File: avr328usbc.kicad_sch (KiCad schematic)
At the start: 10 parts, among them J1 USB_C_Receptacle, J2 USB_C_Receptacle_PowerOnly_6P, U1 ATmega328P-P, U2 MCP2221AxP, U3 ACPL-772L-000E, U4 ACPL-772L-000E

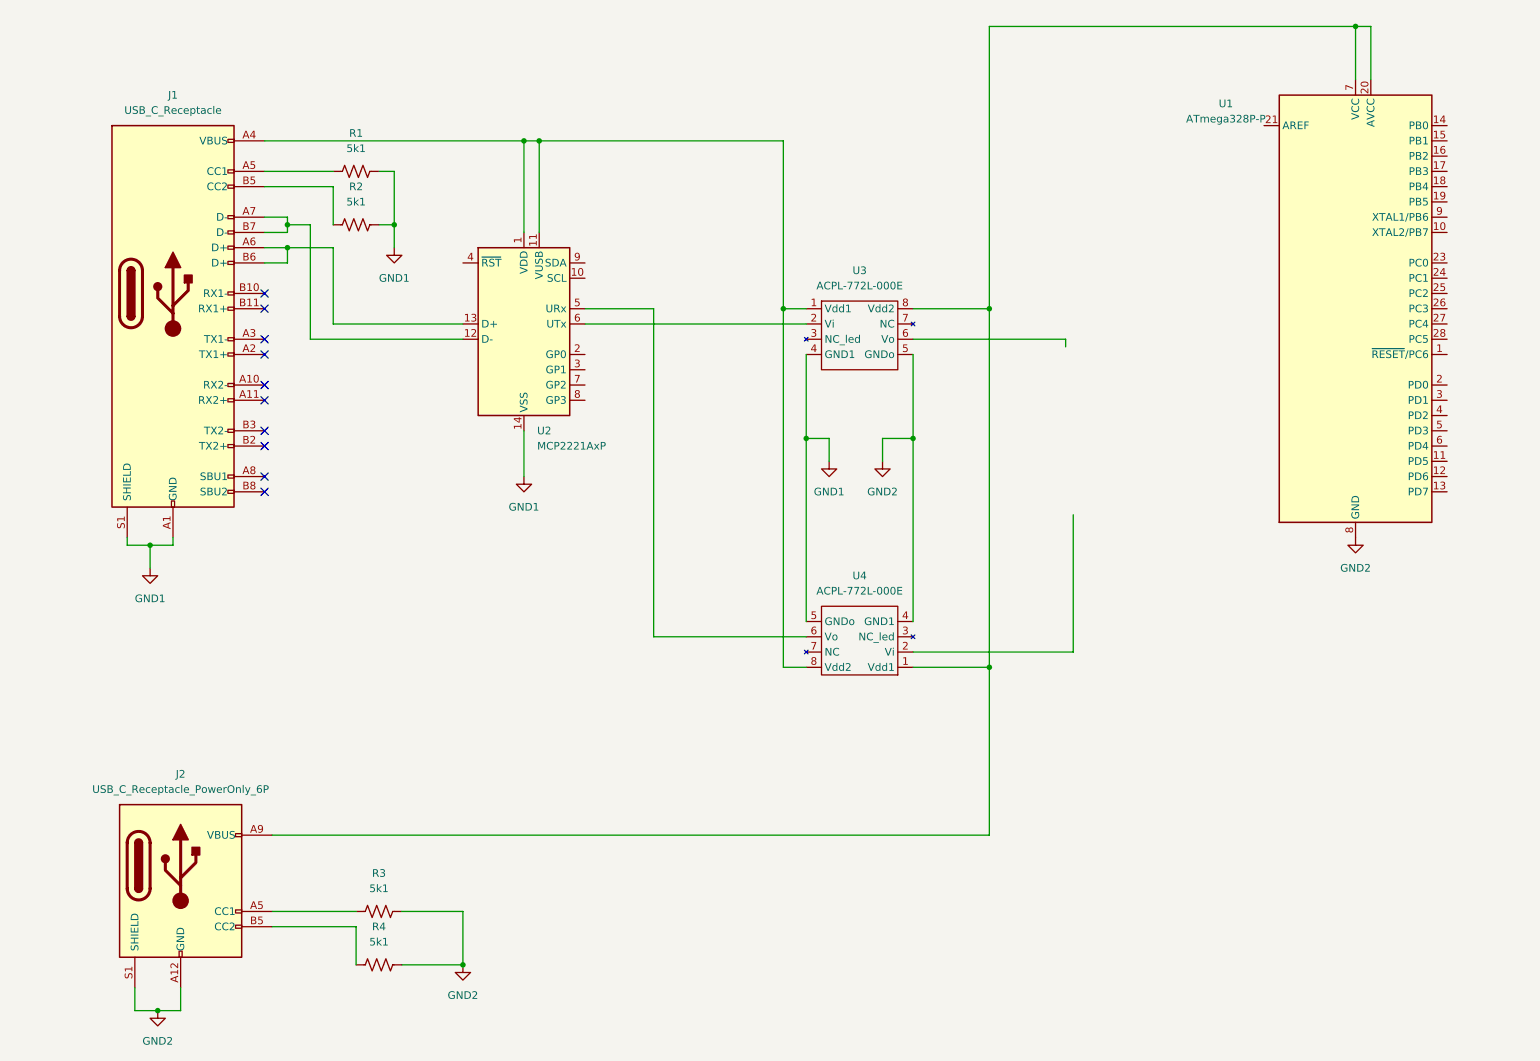
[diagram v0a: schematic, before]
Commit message: schematic: added a bunch of labels & changed pwer to labels
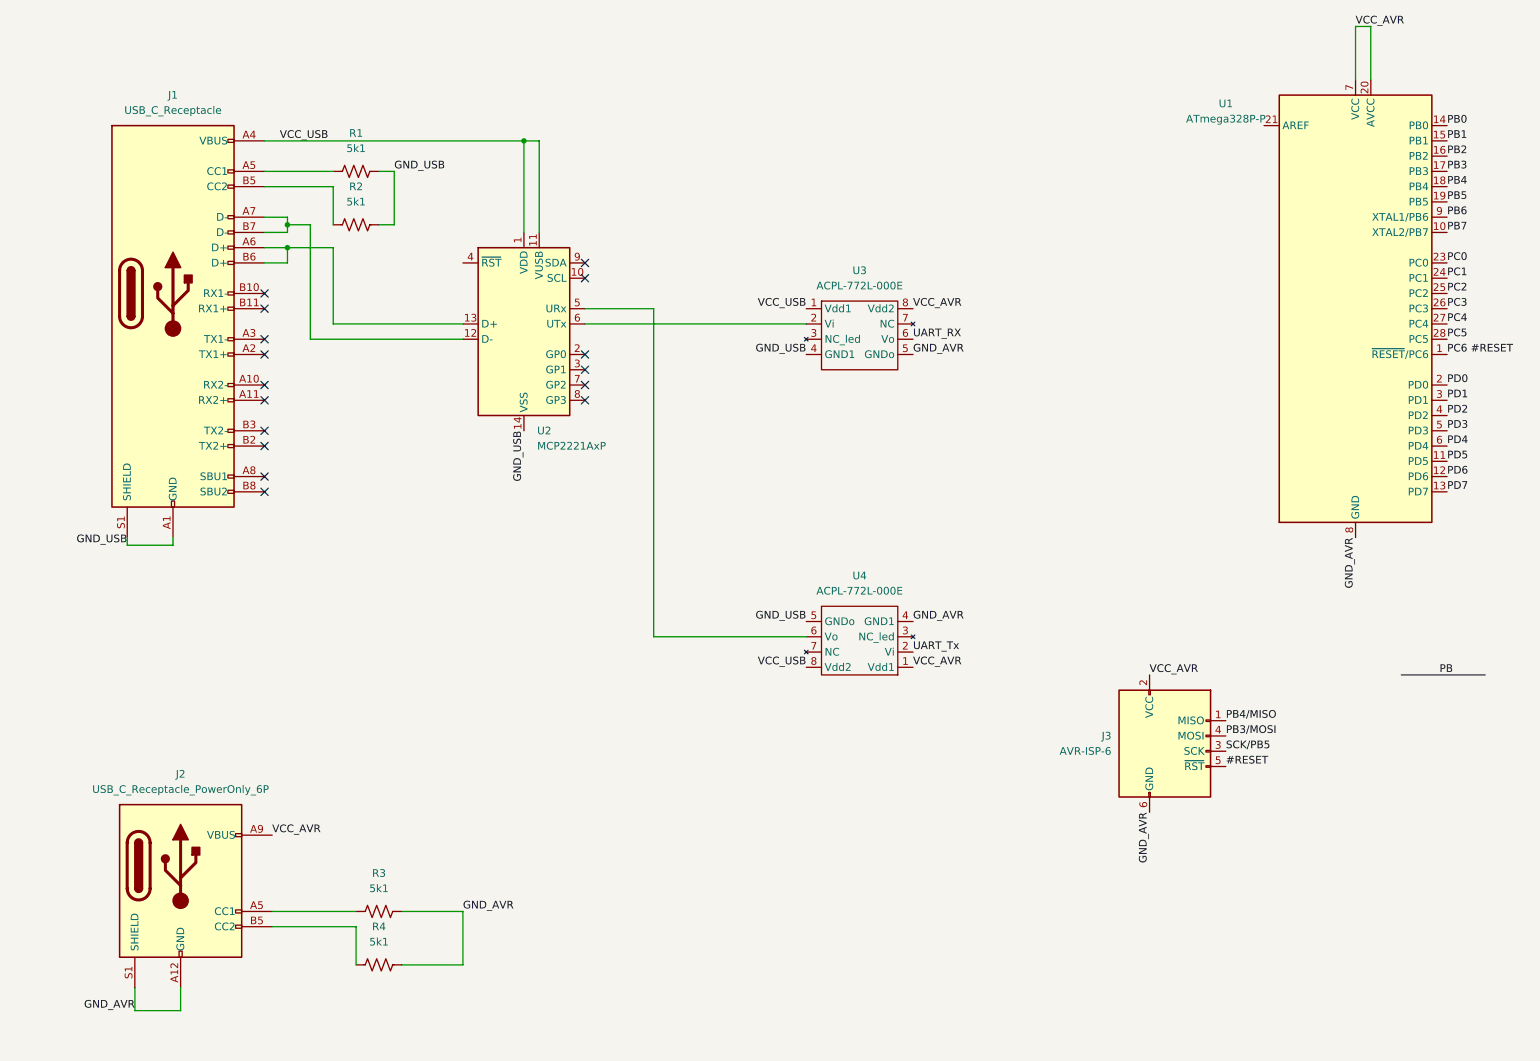
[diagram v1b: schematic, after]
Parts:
- added J3: AVR-ISP-6, symbol Connector:AVR-ISP-6
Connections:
- net VCC_AVR: now reaches J2.A9 (VBUS), J2.B9 (VBUS), U1.20 (AVCC), U1.7 (VCC), U3.8 (Vdd2), U4.1 (Vdd1)
- net VCC_AVR: now also J3.2 (VCC)
- net UART_Tx: now reaches U4.2 (Vi)
- net VCC_USB: now reaches J1.A4 (VBUS), J1.A9 (VBUS), J1.B4 (VBUS), J1.B9 (VBUS), U2.1 (VDD), U2.11 (VUSB), U3.1 (Vdd1), U4.8 (Vdd2)
- net PC6 #RESET: now reaches U1.1 (~{RESET}/PC6)
- net PB7: now reaches U1.10 (XTAL2/PB7)
- net PD5: now reaches U1.11 (PD5)
- net PD6: now reaches U1.12 (PD6)
- net PD7: now reaches U1.13 (PD7)
- net PB0: now reaches U1.14 (PB0)
- net PB1: now reaches U1.15 (PB1)
- net PB2: now reaches U1.16 (PB2)
- net PB3: now reaches U1.17 (PB3)
- net PB4: now reaches U1.18 (PB4)
- net PB5: now reaches U1.19 (PB5)
- net PD0: now reaches U1.2 (PD0)
- net PC0: now reaches U1.23 (PC0)
- net PC1: now reaches U1.24 (PC1)
- net PC2: now reaches U1.25 (PC2)
- net PC3: now reaches U1.26 (PC3)
- net PC4: now reaches U1.27 (PC4)
- net PC5: now reaches U1.28 (PC5)
- net PD1: now reaches U1.3 (PD1)
- net PD2: now reaches U1.4 (PD2)
- net PD3: now reaches U1.5 (PD3)
- net PD4: now reaches U1.6 (PD4)
- net PB6: now reaches U1.9 (XTAL1/PB6)
- net UART_RX: now reaches U3.6 (Vo)
- net GND1 renamed GND_USB
- net GND2 renamed GND_AVR
- net GND_AVR: now also J3.6 (GND)
- new net #RESET: J3.5 (~{RST})
- new net PB3/MOSI: J3.4 (MOSI)
- new net PB4/MISO: J3.1 (MISO)
- new net SCK/PB5: J3.3 (SCK)
- no-connect marks 10 -> 16

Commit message: added mcu sheet and global labels for power
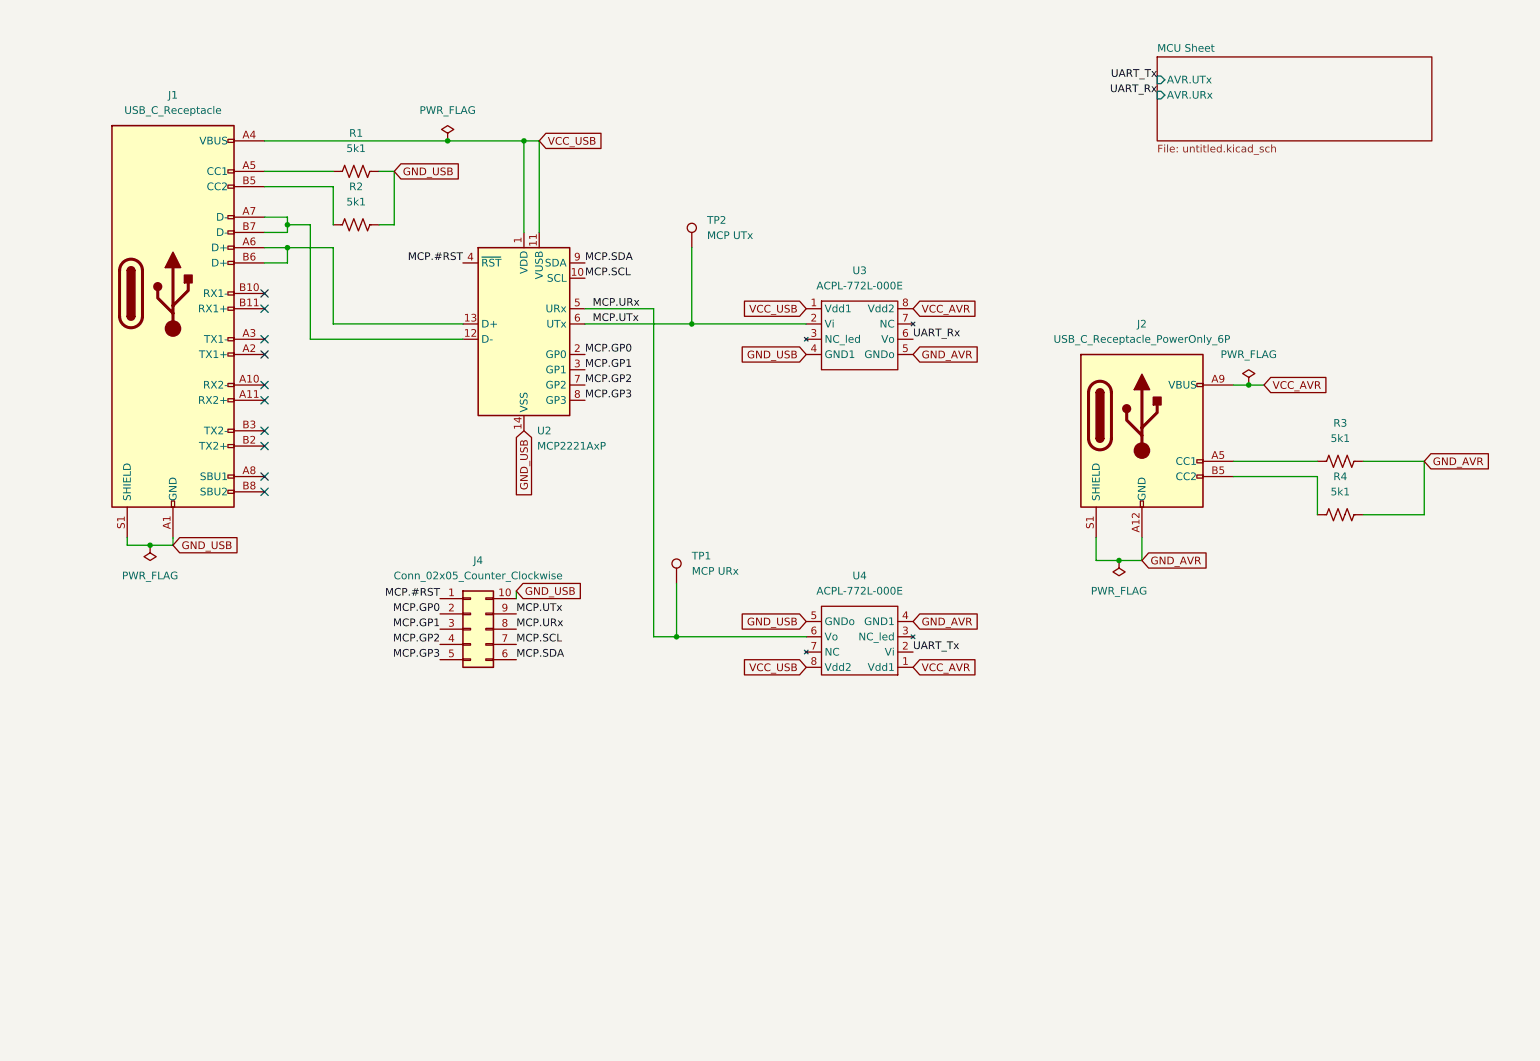
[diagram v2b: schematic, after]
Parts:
- removed J3: AVR-ISP-6, symbol Connector:AVR-ISP-6
- removed U1: ATmega328P-P, Package_DIP:DIP-28_W7.62mm, symbol MCU_Microchip_ATmega:ATmega328P-P
- added J4: Conn_02x05_Counter_Clockwise, symbol Connector_Generic:Conn_02x05_Counter_Clockwise
- added TP1: MCP URx, symbol Connector:TestPoint
- added TP2: MCP UTx, symbol Connector:TestPoint
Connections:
- net GND_USB: now also J4.10 (Pin_10)
- net MCP.URx: now reaches U2.5 (URx), U4.6 (Vo)
- net MCP.URx: now also J4.8 (Pin_8), TP1.1
- net MCP.SCL: now reaches U2.10 (SCL)
- net MCP.SCL: now also J4.7 (Pin_7)
- net MCP.GP0: now reaches U2.2 (GP0)
- net MCP.GP0: now also J4.2 (Pin_2)
- net MCP.GP1: now reaches U2.3 (GP1)
- net MCP.GP1: now also J4.3 (Pin_3)
- net MCP.#RST: now reaches U2.4 (~{RST})
- net MCP.#RST: now also J4.1 (Pin_1)
- net MCP.UTx: now reaches U2.6 (UTx), U3.2 (Vi)
- net MCP.UTx: now also J4.9 (Pin_9), TP2.1
- net MCP.GP2: now reaches U2.7 (GP2)
- net MCP.GP2: now also J4.4 (Pin_4)
- net MCP.GP3: now reaches U2.8 (GP3)
- net MCP.GP3: now also J4.5 (Pin_5)
- net MCP.SDA: now reaches U2.9 (SDA)
- net MCP.SDA: now also J4.6 (Pin_6)
- net UART_RX renamed UART_Rx
- no-connect marks 16 -> 10
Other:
- added sheet MCU Sheet (untitled.kicad_sch)
- company: (none) -> HugonLabs
- title: (none) -> AVR328-USB
- moved on the sheet: J2, R3, R4

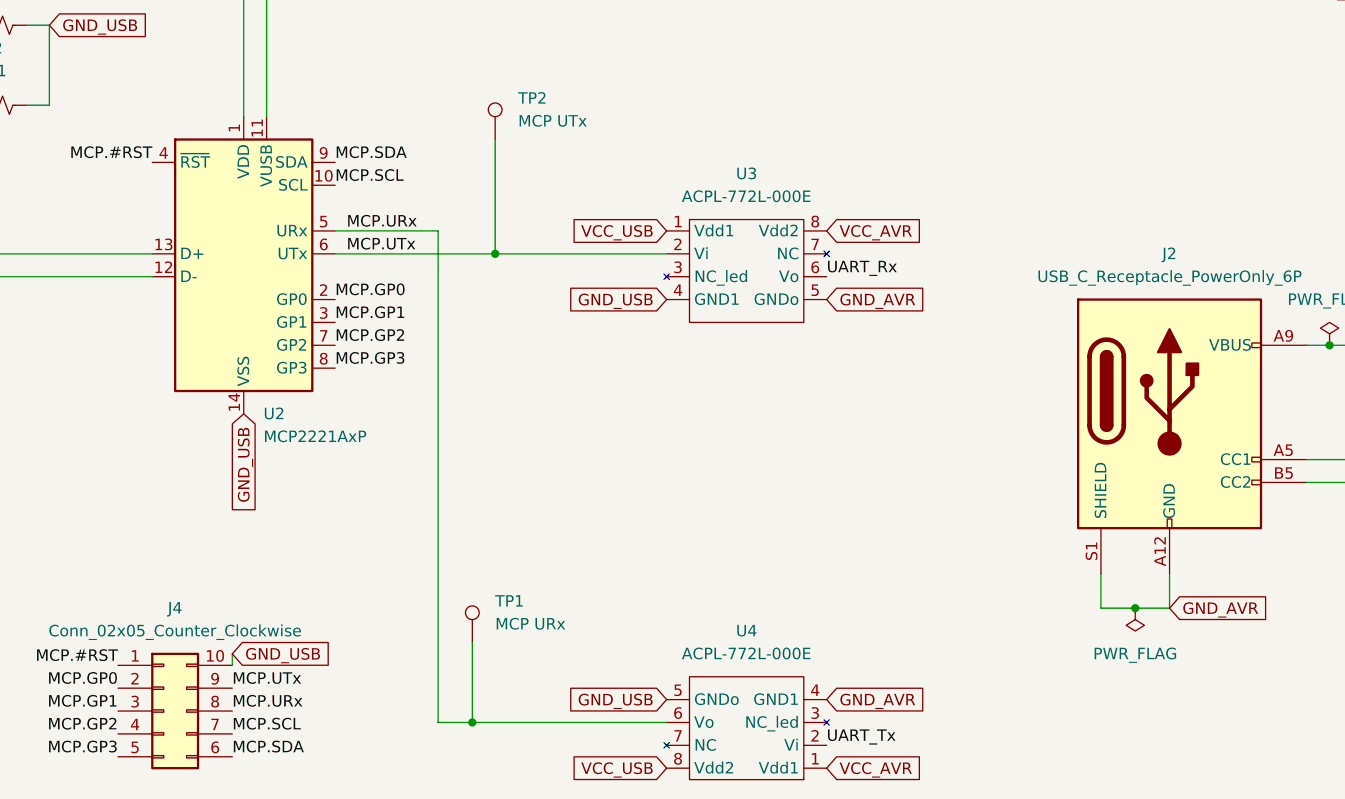
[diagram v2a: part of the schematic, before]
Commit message: sch: finished with main components
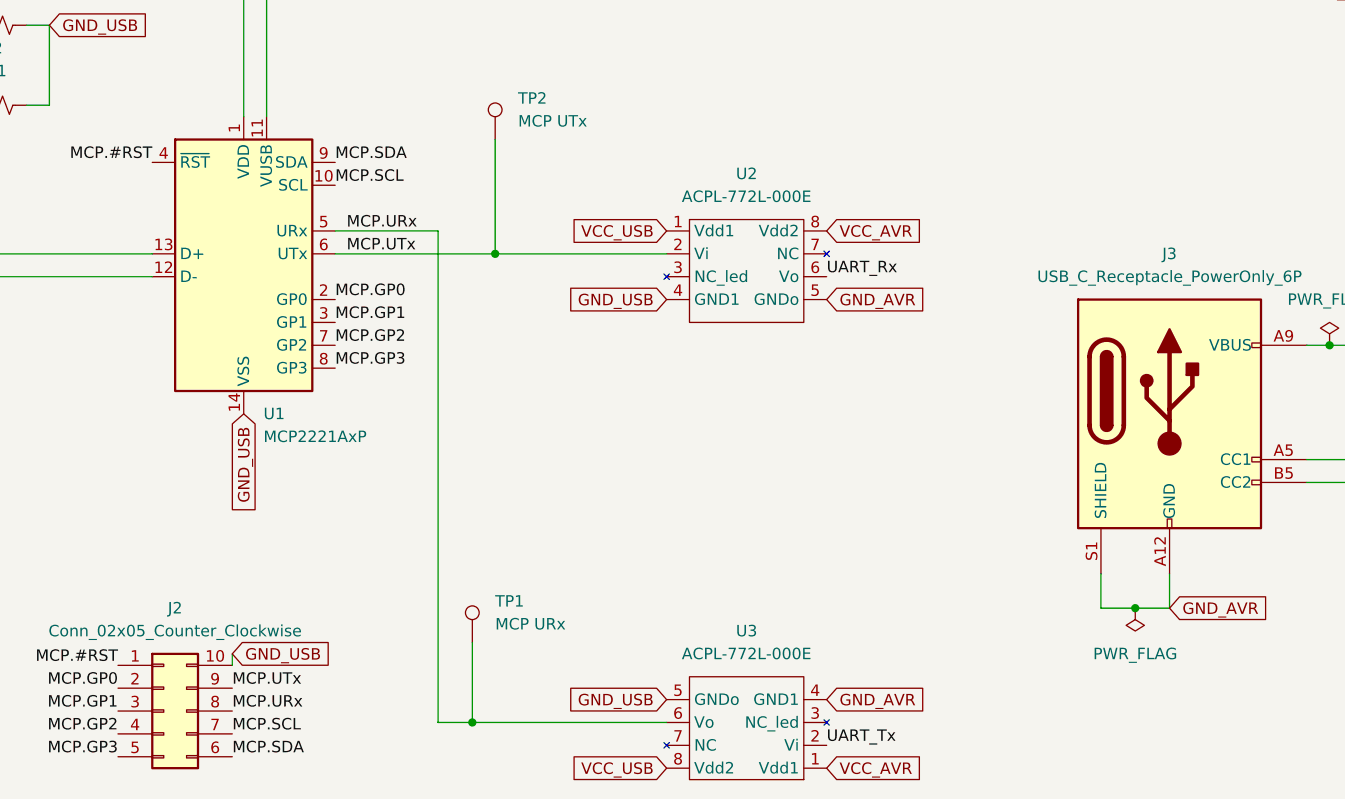
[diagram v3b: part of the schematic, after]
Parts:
- renumbered J4 to J2, J2 to J3, U2 to U1, U3 to U2, U4 to U3
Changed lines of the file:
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@@
 		(dnp no)
 		(fields_autoplaced yes)
-		(property "Reference" "#FLG04"
+		(property "Reference" "#FLG03"
 			(at 204.47 113.665 0)
 			(effects
@@
 			(project "avr328usbc"
 				(path "/e7a067a8-1d75-4b62-a93c-d6508c6150f1"
-					(reference "#FLG04")
+					(reference "#FLG03")
 					(unit 1)
 				)
@@
 		(dnp no)
 		(fields_autoplaced yes)
-		(property "Reference" "J2"
+		(property "Reference" "J3"
 			(at 208.28 72.39 0)
 			(effects
@@
 			(project "avr328usbc"
 				(path "/e7a067a8-1d75-4b62-a93c-d6508c6150f1"
-					(reference "J2")
+					(reference "J3")
 					(unit 1)
 				)
@@
 		(dnp no)
 		(fields_autoplaced yes)
-		(property "Reference" "U4"
+		(property "Reference" "U3"
 			(at 161.29 114.3 0)
 			(effects
@@
 			(project "avr328usbc"
 				(path "/e7a067a8-1d75-4b62-a93c-d6508c6150f1"
-					(reference "U4")
+					(reference "U3")
 					(unit 1)
 				)
@@
 		(dnp no)
 		(fields_autoplaced yes)
-		(property "Reference" "#FLG01"
+		(property "Reference" "#FLG02"
 			(at 92.71 40.005 0)
 			(effects
@@
 			(project "avr328usbc"
 				(path "/e7a067a8-1d75-4b62-a93c-d6508c6150f1"
-					(reference "#FLG01")
+					(reference "#FLG02")
 					(unit 1)
 				)
@@
 		(dnp no)
 		(fields_autoplaced yes)
-		(property "Reference" "U2"
+		(property "Reference" "U1"
 			(at 107.6041 90.17 0)
 			(effects
@@
 			(project "avr328usbc"
 				(path "/e7a067a8-1d75-4b62-a93c-d6508c6150f1"
-					(reference "U2")
+					(reference "U1")
 					(unit 1)
 				)
@@
 		(dnp no)
 		(fields_autoplaced yes)
-		(property "Reference" "J4"
+		(property "Reference" "J2"
 			(at 97.79 111.76 0)
 			(effects
@@
 			(project "avr328usbc"
 				(path "/e7a067a8-1d75-4b62-a93c-d6508c6150f1"
-					(reference "J4")
+					(reference "J2")
 					(unit 1)
 				)
@@
 		(dnp no)
 		(fields_autoplaced yes)
-		(property "Reference" "#FLG03"
+		(property "Reference" "#FLG04"
 			(at 226.06 80.645 0)
 			(effects
@@
 			(project "avr328usbc"
 				(path "/e7a067a8-1d75-4b62-a93c-d6508c6150f1"
-					(reference "#FLG03")
+					(reference "#FLG04")
 					(unit 1)
 				)
@@
 		(dnp no)
 		(fields_autoplaced yes)
-		(property "Reference" "U3"
+		(property "Reference" "U2"
 			(at 161.29 63.5 0)
 			(effects
@@
 			(project "avr328usbc"
 				(path "/e7a067a8-1d75-4b62-a93c-d6508c6150f1"
-					(reference "U3")
+					(reference "U2")
 					(unit 1)
 				)
@@
 		(dnp no)
 		(fields_autoplaced yes)
-		(property "Reference" "#FLG02"
+		(property "Reference" "#FLG01"
 			(at 43.18 111.125 0)
 			(effects
@@
 			(project "avr328usbc"
 				(path "/e7a067a8-1d75-4b62-a93c-d6508c6150f1"
-					(reference "#FLG02")
-					(unit 1)
-				)
+					(reference "#FLG01")
+					(unit 1)
+				)
